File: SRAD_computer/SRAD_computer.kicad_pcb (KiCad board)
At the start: 2 copper layers, 32 parts, among them J1 USB_B_Micro, J2 Conn_01x02, U1 NCP1117-3.3_SOT223, U2 W25Q128JVS, U3 RP2040, Y1 ABM8-272-T3

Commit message: PCB placement
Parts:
- added C_BME_VDD1: 100n, TCLib:C_0805, F.Cu at (45.2, 74.7)
- added C_BME_VDDIO1: 100n, TCLib:C_0805, F.Cu at (45.2, 80.7)
- added C_MPU_REG1: 100n, TCLib:C_0805, F.Cu at (111.3, 44.1)
- added C_MPU_VDD: 100n, TCLib:C_0805, F.Cu at (113.2, 40.5)
- added C_MPU_VDDIO: 10n, TCLib:C_0805, F.Cu at (106.8, 44.0)
- added C_SAM_VBCKP1: C, TCLib:C_0805, F.Cu at (75.1, 82.2)
- added C_SAM_VCC1: C, TCLib:C_0805, F.Cu at (89.2, 70.5)
- added C_SAM_VCCIO1: C, TCLib:C_0805, F.Cu at (75.1, 77.7)
- added R_BME_SCL1: R, TCLib:R_0805, F.Cu at (54.2, 77.9)
- added R_BME_SDA1: R, TCLib:R_0805, F.Cu at (50.3, 77.9)
- added R_MPU_SCL1: R, TCLib:R_0805, F.Cu at (109.2, 35.6)
- added R_MPU_SDA1: R, TCLib:R_0805, F.Cu at (105.6, 35.7)
- added R_SAM_SCL1: R, TCLib:R_0805, F.Cu at (90.3, 92.6)
- added R_SAM_SDA1: R, TCLib:R_0805, F.Cu at (90.3, 95.6)
- added U4: BME280, my_lib:PSON65P250X250X100-8N, F.Cu at (46.7, 77.7)
- added U5: MPU-9250, my_lib:MPU-9250, F.Cu at (108.8, 40.5)
- added U6: SAM-M8Q-0-10, my_lib:MODULE_SAM-M8Q-0-10, F.Cu at (86.1, 81.0)
- R1, R2: footprint Resistor_SMD:R_0402_1005Metric -> Resistor_SMD:R_0805_2012Metric
- moved H3 89.3 mm to (127.0, 97.0)
- moved H2 72.7 mm to (128.0, 16.0)
- moved H4 53.8 mm to (16.0, 97.5)
- moved C10 35.5 mm to (62.0, 47.1)
- moved C11 35.5 mm to (67.2, 45.2)
- moved C12 35.5 mm to (70.8, 45.2)
- moved C13 35.5 mm to (77.4, 51.7)
- moved C14 35.5 mm to (70.8, 58.0)
- moved C17 35.5 mm to (77.8, 42.5)
- moved C2 35.5 mm to (81.7, 60.4)
- moved C3 35.5 mm to (81.7, 58.4)
- moved C4 35.5 mm to (63.3, 42.2)
- moved C5 35.5 mm to (56.0, 60.9)
- moved C6 35.5 mm to (77.4, 50.4)
- moved C8 35.5 mm to (62.0, 49.0)
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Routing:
- net +3V3: track 0.00 -> 38.9 mm
- net GND: track 0.00 -> 30.9 mm
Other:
- board text added: "Acc & Gyro"
- board text added: "GPS"

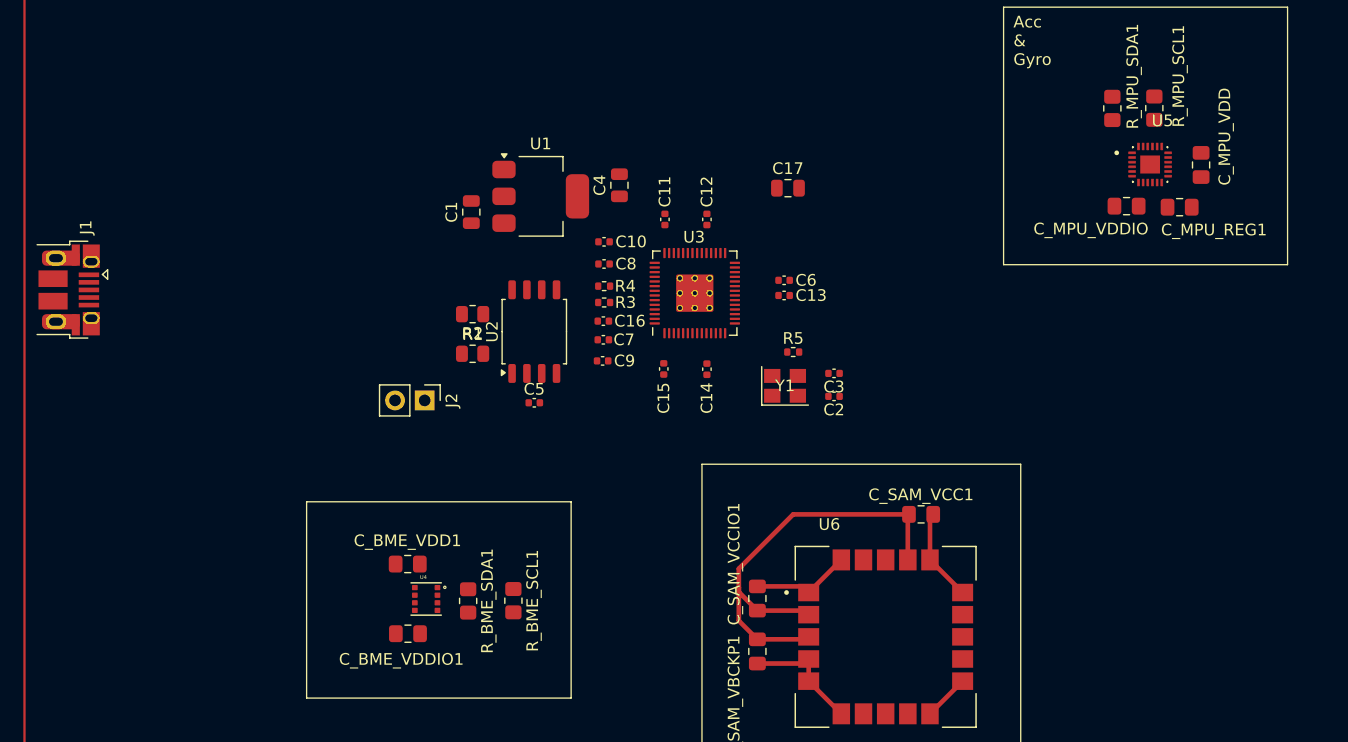
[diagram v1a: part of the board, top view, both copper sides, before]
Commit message: RP2040 decoupling capacitors and resistances connection
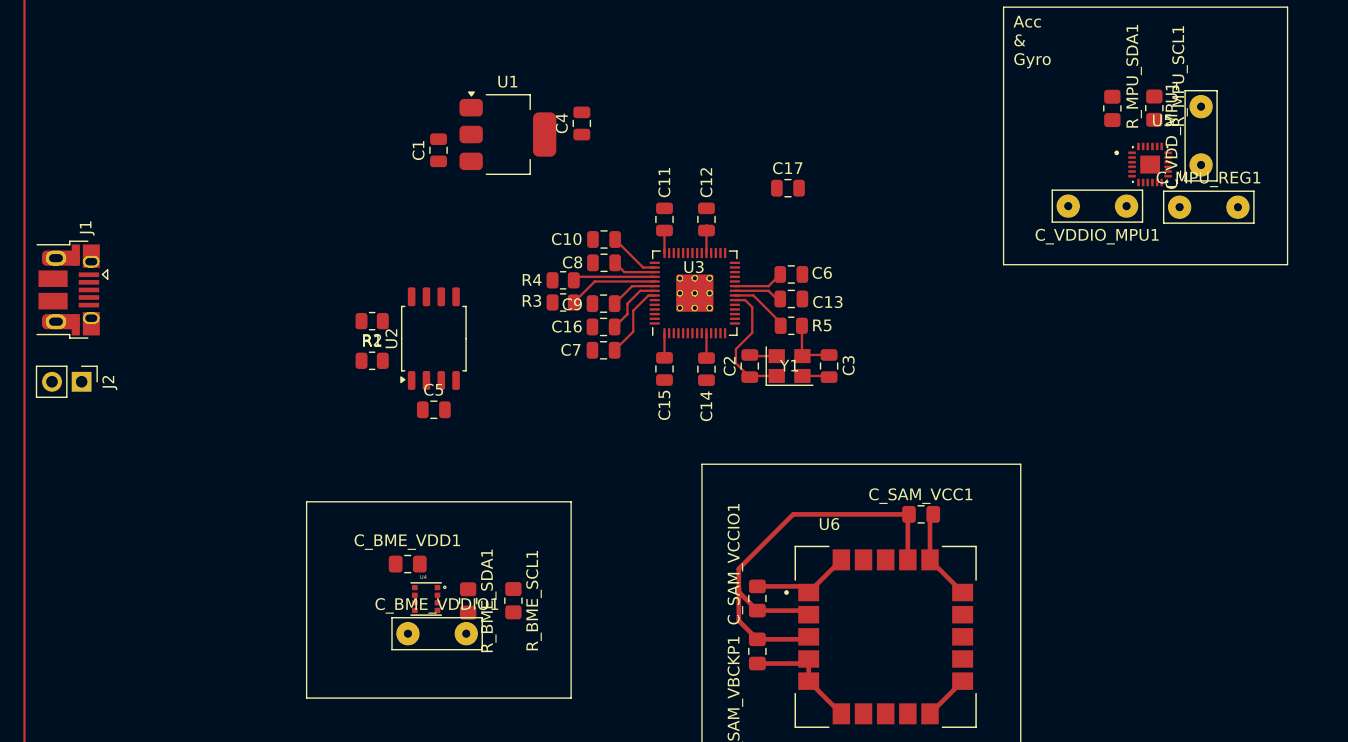
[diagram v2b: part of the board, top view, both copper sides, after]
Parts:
- C10, C11, C12, C13, C14, C15, C16, C2, C3, C5, C6, C7, C8, C9: footprint Capacitor_SMD:C_0402_1005Metric -> Capacitor_SMD:C_0805_2012Metric
- C_BME_VDDIO1, C_MPU_REG1: footprint TCLib:C_0805 -> TCLib:C_5mm
- C_VDDIO_MPU1: renamed from C_MPU_VDDIO; footprint TCLib:C_0805 -> TCLib:C_5mm
- C_VDD_MPU1: renamed from C_MPU_VDD; footprint TCLib:C_0805 -> TCLib:C_5mm
- R3, R4, R5: footprint Resistor_SMD:R_0402_1005Metric -> Resistor_SMD:R_0805_2012Metric
- moved J2 29.5 mm to (17.2, 59.1)
- moved C5 8.63 mm to (47.4, 61.5)
- moved U2 8.63 mm to (47.4, 55.4)
- moved R1 8.63 mm to (42.1, 57.3)
- moved R2 8.63 mm to (42.1, 53.9)
- moved C2 7.68 mm to (74.5, 57.8), turned to 90 degrees
- moved C4 6.20 mm to (60.1, 37.0)
- moved U1 6.00 mm to (53.8, 37.9)
- moved C1 6.00 mm to (47.8, 39.2)
- moved C9 4.91 mm to (62.0, 52.4)
- moved R4 3.55 mm to (58.5, 50.4)
- moved R3 3.52 mm to (58.5, 52.3)
- moved R5 2.26 mm to (78.0, 54.3)
- moved Y1 1.74 mm to (77.9, 57.8)
- moved C7 0.90 mm to (62.0, 56.4)
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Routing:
- net +3V3: track 38.9 -> 64.9 mm
- net +1V1: track 0.00 -> 14.5 mm
- net /XIN: track 0.00 -> 11.2 mm
- net Net-(U3-USB_DP): track 0.00 -> 7.68 mm
- net Net-(U3-USB_DM): track 0.00 -> 7.06 mm
- net /XOUT: track 0.00 -> 5.16 mm
- net GND: track 30.9 -> 35.9 mm
- net Net-(C3-Pad1): track 0.00 -> 4.94 mm

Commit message: update PCB
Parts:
- C_BME_VDDIO1, C_MPU_REG1, C_VDDIO_MPU1, C_VDD_MPU1: footprint TCLib:C_5mm -> TCLib:C_0805
- H1, H2, H3, H4: footprint MountingHole:MountingHole_2.7mm_M2.5 -> MountingHole:MountingHole_3.5mm
- moved R_MPU_SCL1 39.4 mm to (70.4, 42.8), turned to 0 degrees
- moved C_VDD_MPU1 37.8 mm to (75.5, 42.9), turned to 180 degrees
- moved R_MPU_SDA1 36.7 mm to (70.5, 46.4), turned to 0 degrees
- moved U5 33.7 mm to (75.7, 46.5), turned to 90 degrees
- moved C_MPU_REG1 31.8 mm to (79.6, 43.7), turned to 90 degrees
- moved C_VDDIO_MPU1 27.6 mm to (79.6, 48.3), turned to -90 degrees
- moved R_SAM_SCL1 25.8 mm to (81.6, 68.4), turned to -90 degrees
- moved R_SAM_SDA1 23.7 mm to (81.6, 73.5), turned to -90 degrees
- moved C1 22.0 mm to (26.9, 45.9)
- moved U1 22.0 mm to (32.8, 44.5)
- moved C_SAM_VBCKP1 19.7 mm to (60.4, 69.1)
- moved C_SAM_VCCIO1 19.7 mm to (60.4, 64.5)
- moved C_SAM_VCC1 19.7 mm to (74.5, 57.3)
- moved U6 19.7 mm to (71.4, 67.8)
- moved C4 19.3 mm to (41.7, 42.7)
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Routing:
- net +3V3: track 64.9 -> 47.1 mm
- net +1V1: track 14.5 -> 0.00 mm
- net Net-(U3-USB_DP): track 7.68 -> 0.00 mm
- net Net-(U3-USB_DM): track 7.06 -> 0.00 mm
- net /XOUT: track 5.16 -> 0.00 mm
- net /XIN: track 11.2 -> 6.29 mm
- net Net-(C3-Pad1): track 4.94 -> 2.38 mm
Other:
- board text added: "+x"
- board text added: "+y"
- board text removed: "Acc & Gyro"
- board text removed: "GPS"

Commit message: PCB Update
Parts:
- moved C_SAM_VBCKP1 5.83 mm to (65.9, 67.1)
- moved C_SAM_VCCIO1 5.83 mm to (65.9, 62.5)
- moved R_SAM_SCL1 5.83 mm to (87.1, 66.3)
- moved R_SAM_SDA1 5.83 mm to (87.1, 71.5)
- moved U6 5.83 mm to (76.9, 65.8)
- moved C_SAM_VCC1 5.83 mm to (79.9, 55.3)
- moved C_BME_VDD1 5.30 mm to (53.7, 72.6)
- moved C_BME_VDDIO1 5.30 mm to (59.2, 72.6)
- moved U4 5.30 mm to (55.9, 69.4)
- moved R_BME_SCL1 5.30 mm to (55.9, 62.1)
- moved R_BME_SDA1 5.30 mm to (55.9, 66.0)
- moved C5 4.64 mm to (41.5, 65.8)
- moved R2 4.64 mm to (48.6, 65.9)
- moved U2 4.64 mm to (45.2, 60.6)
- moved R1 4.64 mm to (45.0, 65.8)
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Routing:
- net +3V3: track 47.1 -> 84.1 mm
- net /QSPI_SD3: track 0.00 -> 23.7 mm
- net /QSPI_SCLK: track 0.00 -> 21.6 mm
- net /QSPI_SD0: track 0.00 -> 18.5 mm
- net /QSPI_SS: track 0.00 -> 13.0 mm
- net /QSPI_SD1: track 0.00 -> 12.4 mm
- net /QSPI_SD2: track 0.00 -> 11.8 mm
- net +1V1: track 0.00 -> 10.1 mm
- net Net-(U3-USB_DM): track 0.00 -> 9.40 mm
- net Net-(U3-USB_DP): track 0.00 -> 8.66 mm

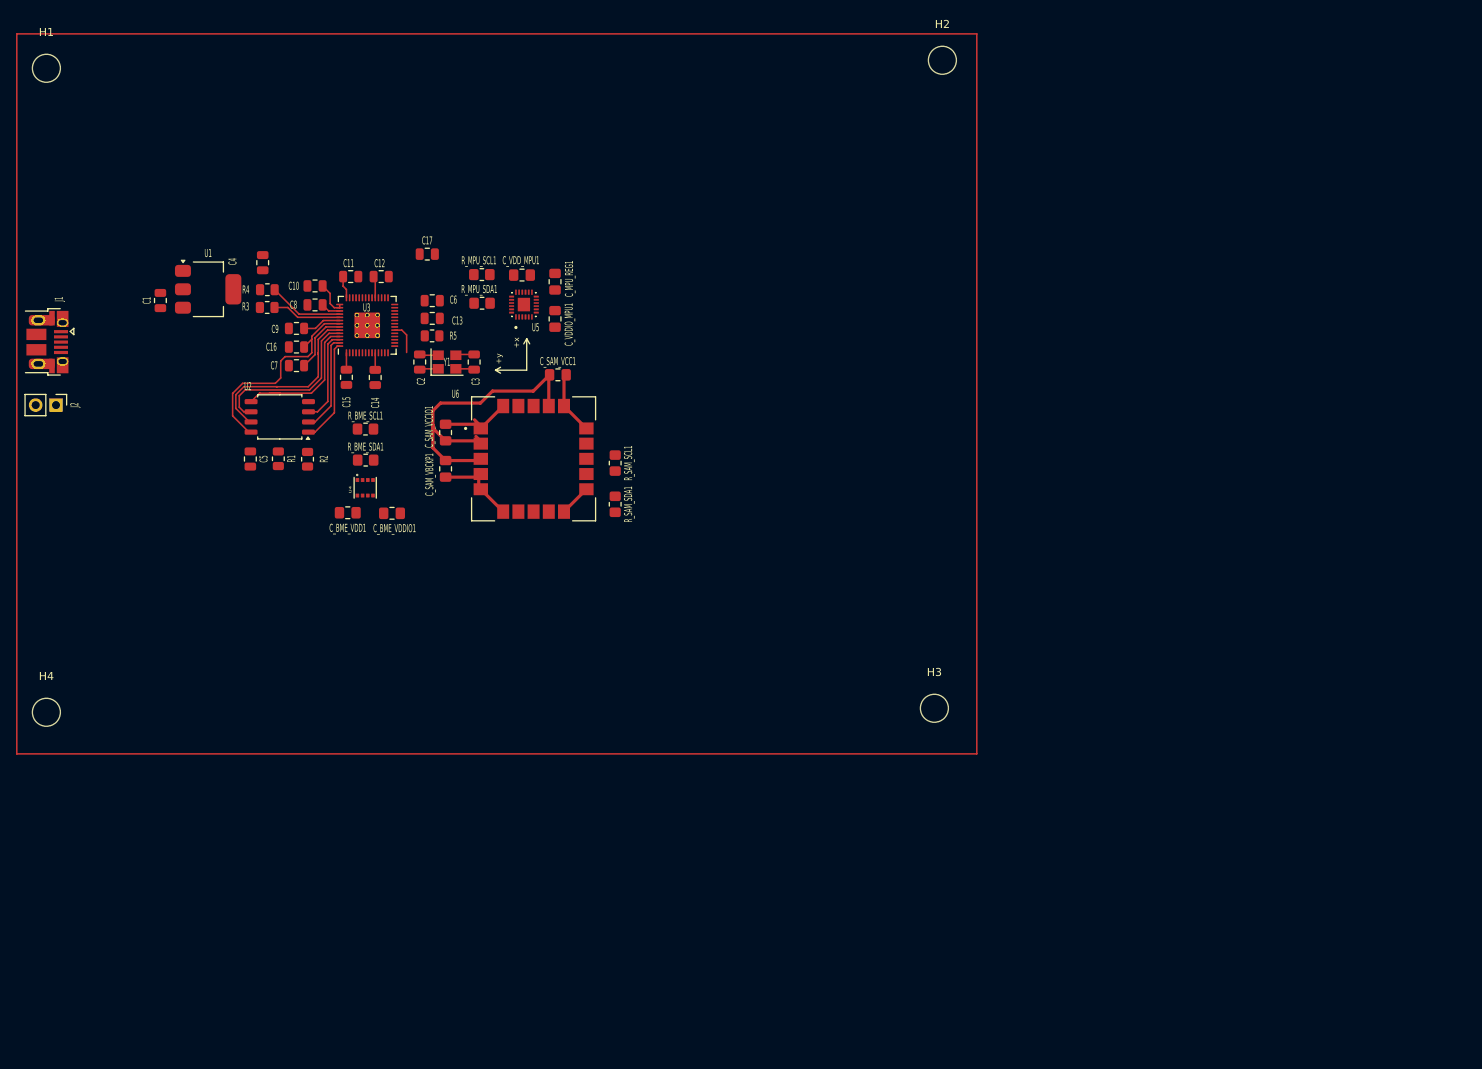
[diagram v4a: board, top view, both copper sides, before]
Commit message: Change Layout: Shield for GPS
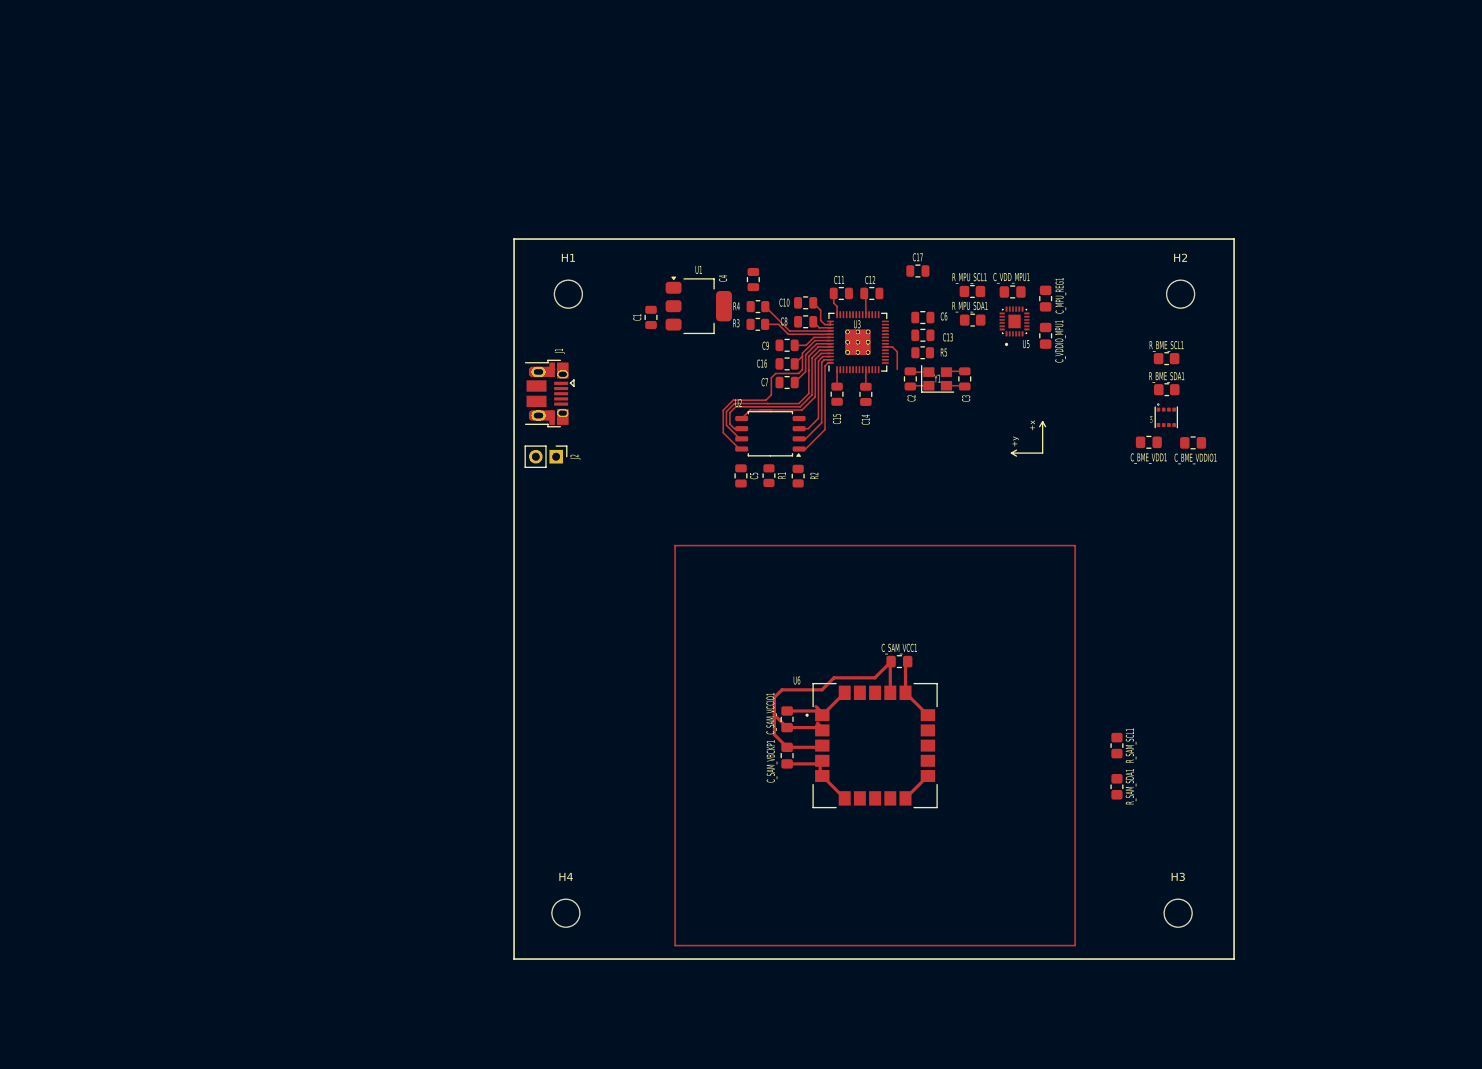
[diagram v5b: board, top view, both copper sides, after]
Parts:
- moved R_BME_SDA1 100.5 mm to (156.0, 57.2)
- moved U4 100.5 mm to (156.0, 60.6)
- moved C_BME_VDD1 100.5 mm to (153.8, 63.8)
- moved C_BME_VDDIO1 100.5 mm to (159.3, 63.8)
- moved R_BME_SCL1 100.5 mm to (156.0, 53.3)
- moved R_SAM_SCL1 72.0 mm to (149.8, 101.7)
- moved R_SAM_SDA1 72.0 mm to (149.8, 106.8)
- moved H1 71.1 mm to (81.2, 45.2)
- moved H4 69.6 mm to (80.9, 122.6)
- moved J1 62.8 mm to (77.5, 57.7)
- moved J2 62.8 mm to (79.7, 65.6)
- moved U5 61.4 mm to (137.0, 48.6)
- moved C11 61.4 mm to (115.4, 45.1)
- moved C14 61.4 mm to (118.4, 57.8)
- moved C16 61.4 mm to (108.6, 54.0)
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
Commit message: Changed board size & GPS shielding
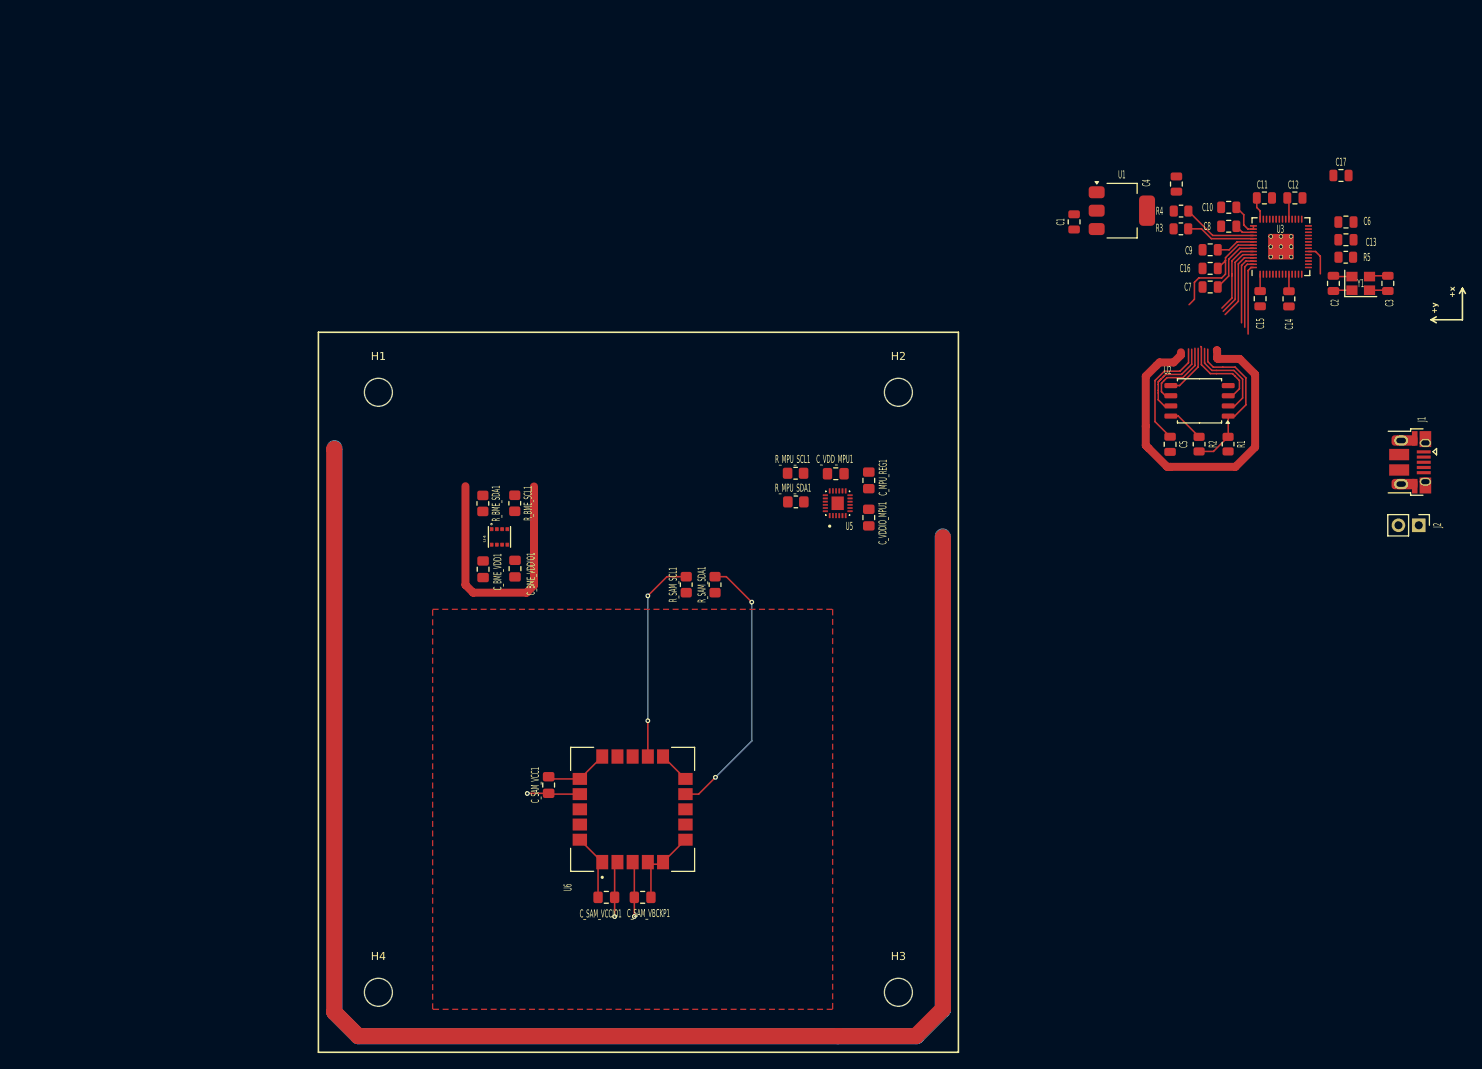
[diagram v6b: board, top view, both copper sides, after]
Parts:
- moved J1 108.2 mm to (185.3, 66.2)
- moved J2 108.2 mm to (187.5, 74.1)
- moved R_BME_SDA1 86.7 mm to (70.6, 71.4), turned to -90 degrees
- moved C_BME_VDDIO1 86.2 mm to (74.6, 79.5), turned to -90 degrees
- moved C_BME_VDD1 84.7 mm to (70.6, 79.6), turned to -90 degrees
- moved U4 84.7 mm to (72.6, 75.6)
- moved R_BME_SCL1 83.5 mm to (74.5, 71.4), turned to -90 degrees
- moved R1 57.5 mm to (163.7, 64.0)
- moved R_SAM_SCL1 57.5 mm to (96.0, 81.6), turned to 90 degrees
- moved R_SAM_SDA1 56.2 mm to (99.6, 81.6), turned to 90 degrees
- moved C3 54.2 mm to (183.7, 43.9)
- moved C1 54.2 mm to (144.5, 36.2)
- moved C12 54.2 mm to (172.1, 33.2)
- moved C15 54.2 mm to (167.7, 45.8)
- moved R3 54.2 mm to (157.8, 37.1)
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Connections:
- C_SAM_VBCKP1 pad 2: GND -> Net-(U6-SDA)
- C_SAM_VCC1 pad 2: GND -> Net-(U6-SDA)
- C_SAM_VCCIO1 pad 2: GND -> Net-(U6-SDA)
- U6 pad 1: GND -> Net-(U6-SDA)
- U6 pad 10: GND -> Net-(U6-SDA)
- U6 pad 11: GND -> Net-(U6-SDA)
- U6 pad 15: GND -> Net-(U6-SDA)
- U6 pad 16: GND -> Net-(U6-SDA)
- U6 pad 20: GND -> Net-(U6-SDA)
- U6 pad 4: GND -> Net-(U6-SDA)
- U6 pad 5: GND -> Net-(U6-SDA)
- U6 pad 6: GND -> Net-(U6-SDA)
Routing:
- net GND: track 35.9 -> 293.1 mm
- net (no net): track 0.00 -> 208.4 mm
- net Net-(U6-SDA): track 0.00 -> 64.5 mm, vias 0 -> 2
- net Net-(U6-SCL): track 0.00 -> 25.9 mm, vias 0 -> 2
- net /QSPI_SS: track 13.0 -> 29.1 mm
- net +3V3: track 84.1 -> 72.5 mm, vias 0 -> 3
- net /QSPI_SD1: track 12.4 -> 20.7 mm
- net /QSPI_SD2: track 11.8 -> 19.5 mm
- net /QSPI_SD3: track 23.7 -> 20.9 mm
- net /QSPI_SD0: track 18.5 -> 15.9 mm
- net /QSPI_SCLK: track 21.6 -> 19.1 mm
- added copper zone on F.Cu, net GND
